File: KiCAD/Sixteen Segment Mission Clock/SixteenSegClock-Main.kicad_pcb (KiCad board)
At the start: 2 copper layers, 114.3 x 165.1 mm, 0 parts

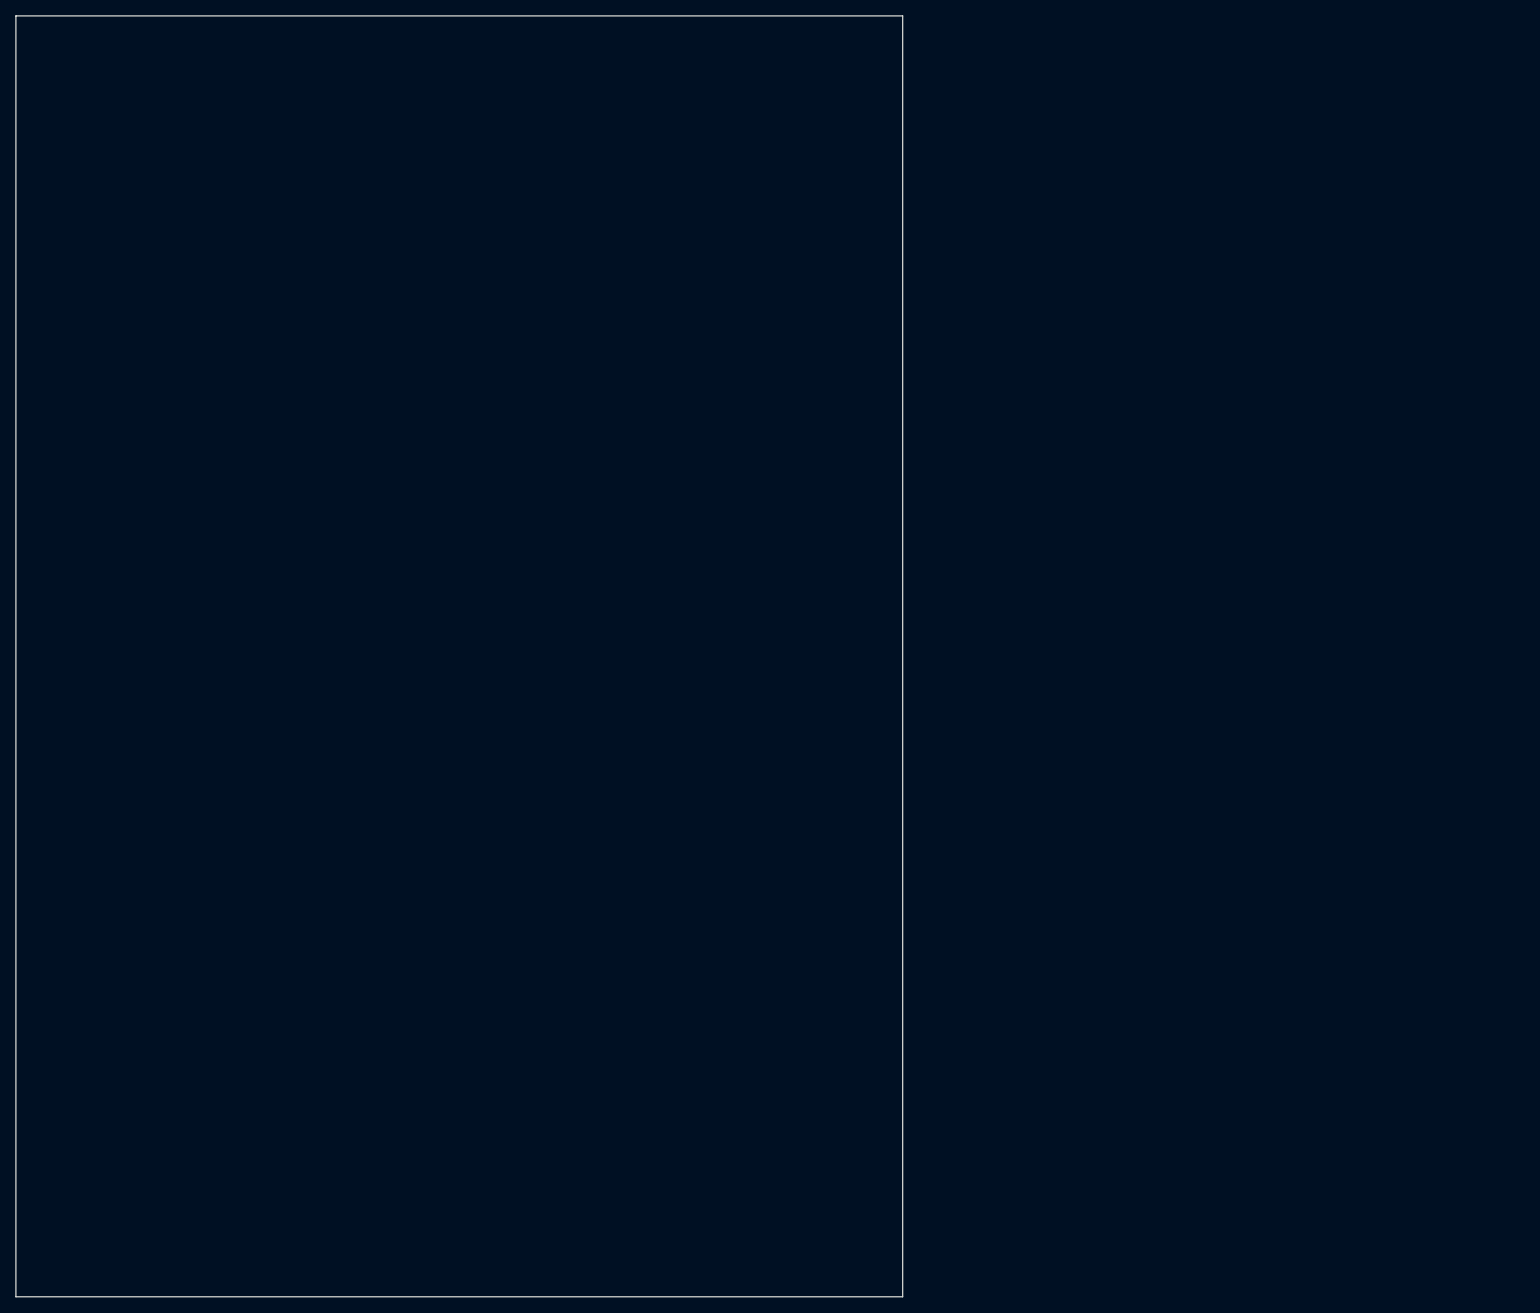
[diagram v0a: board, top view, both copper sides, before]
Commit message: Placed LEDs
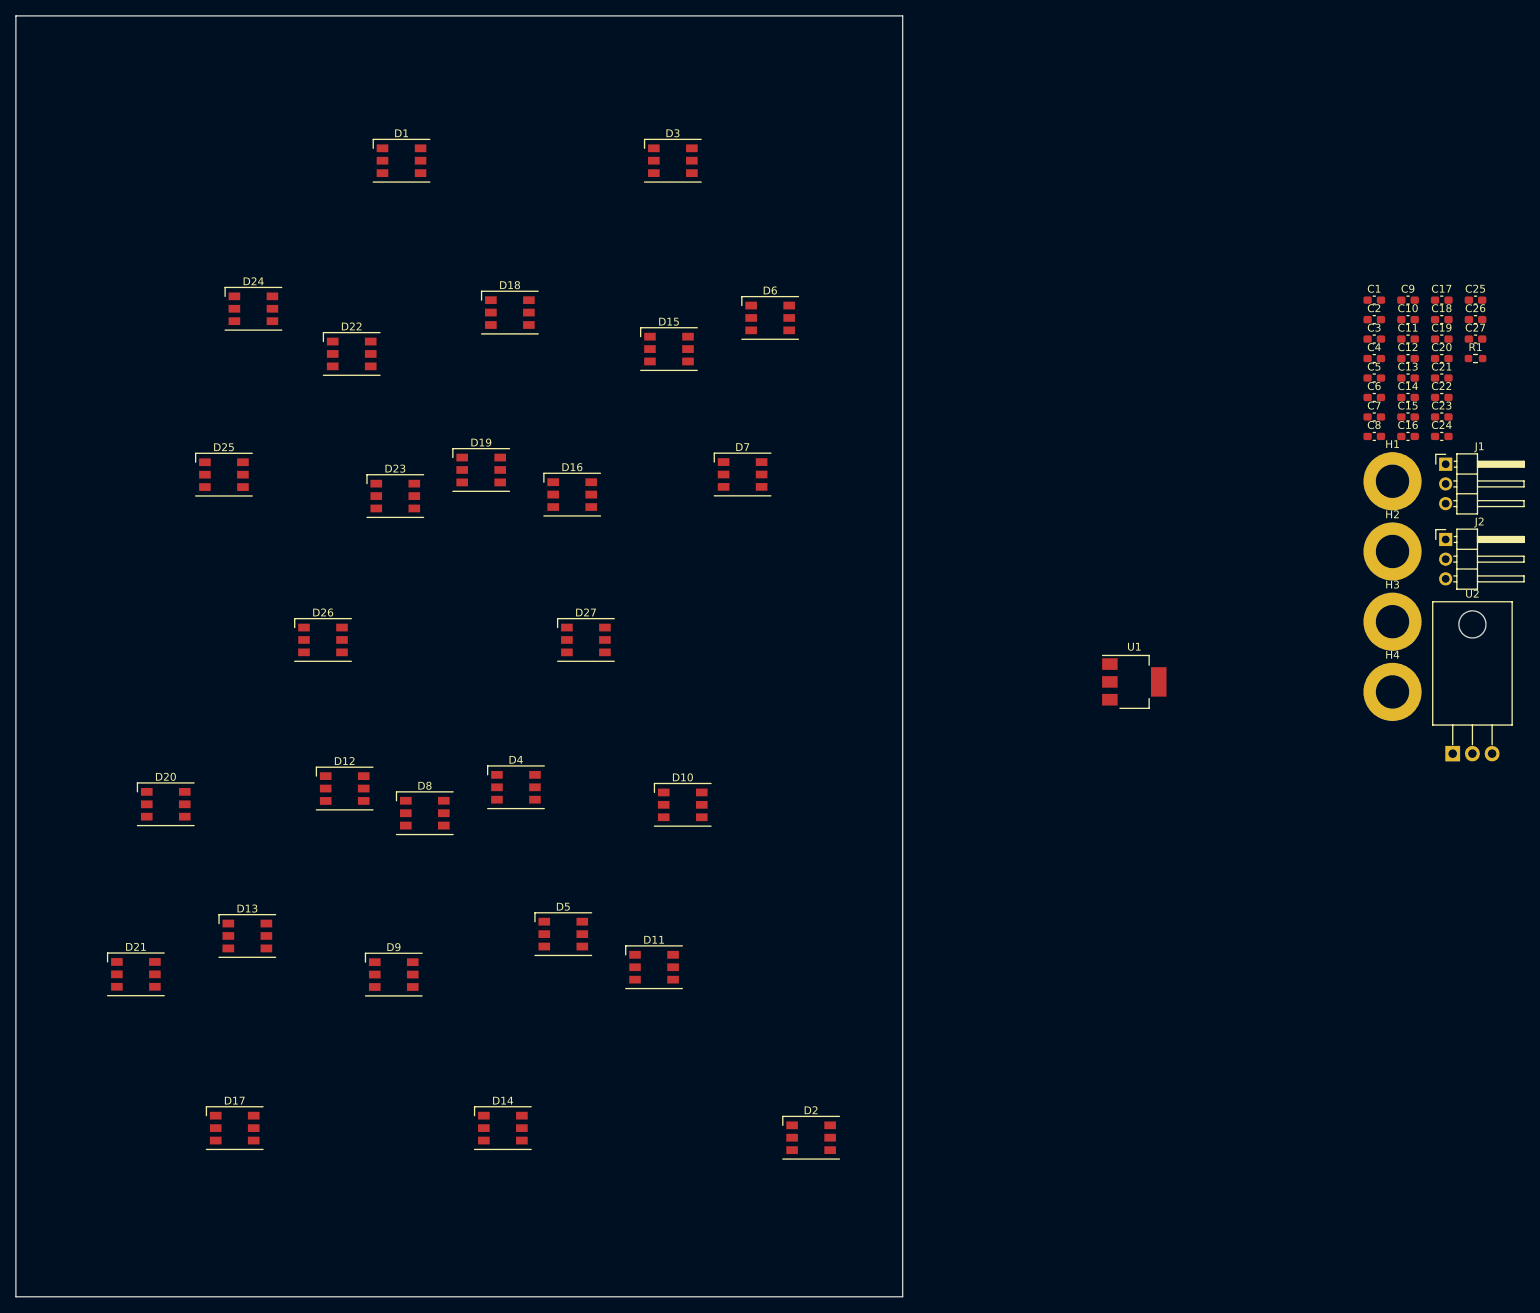
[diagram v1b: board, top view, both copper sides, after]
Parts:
- added C1: 1uF, Capacitor_SMD:C_0603_1608Metric_Pad1.08x0.95mm_HandSolder, F.Cu at (214.0, 65.0)
- added C10: 10uF, Capacitor_SMD:C_0603_1608Metric_Pad1.08x0.95mm_HandSolder, F.Cu at (218.4, 67.5)
- added C11: 10uF, Capacitor_SMD:C_0603_1608Metric_Pad1.08x0.95mm_HandSolder, F.Cu at (218.4, 70.1)
- added C12: 1uF, Capacitor_SMD:C_0603_1608Metric_Pad1.08x0.95mm_HandSolder, F.Cu at (218.4, 72.6)
- added C13: 1uF, Capacitor_SMD:C_0603_1608Metric_Pad1.08x0.95mm_HandSolder, F.Cu at (218.4, 75.1)
- added C14: 1uF, Capacitor_SMD:C_0603_1608Metric_Pad1.08x0.95mm_HandSolder, F.Cu at (218.4, 77.6)
- added C15: 1uF, Capacitor_SMD:C_0603_1608Metric_Pad1.08x0.95mm_HandSolder, F.Cu at (218.4, 80.1)
- added C16: 1uF, Capacitor_SMD:C_0603_1608Metric_Pad1.08x0.95mm_HandSolder, F.Cu at (218.4, 82.6)
- added C17: 1uF, Capacitor_SMD:C_0603_1608Metric_Pad1.08x0.95mm_HandSolder, F.Cu at (222.7, 65.0)
- added C18: 1uF, Capacitor_SMD:C_0603_1608Metric_Pad1.08x0.95mm_HandSolder, F.Cu at (222.7, 67.5)
- added C19: 1uF, Capacitor_SMD:C_0603_1608Metric_Pad1.08x0.95mm_HandSolder, F.Cu at (222.7, 70.1)
- added C2: 1uF, Capacitor_SMD:C_0603_1608Metric_Pad1.08x0.95mm_HandSolder, F.Cu at (214.0, 67.5)
- added C20: 1uF, Capacitor_SMD:C_0603_1608Metric_Pad1.08x0.95mm_HandSolder, F.Cu at (222.7, 72.6)
- added C21: 1uF, Capacitor_SMD:C_0603_1608Metric_Pad1.08x0.95mm_HandSolder, F.Cu at (222.7, 75.1)
- added C22: 1uF, Capacitor_SMD:C_0603_1608Metric_Pad1.08x0.95mm_HandSolder, F.Cu at (222.7, 77.6)
- added C23: 1uF, Capacitor_SMD:C_0603_1608Metric_Pad1.08x0.95mm_HandSolder, F.Cu at (222.7, 80.1)
- added C24: 1uF, Capacitor_SMD:C_0603_1608Metric_Pad1.08x0.95mm_HandSolder, F.Cu at (222.7, 82.6)
- added C25: 1uF, Capacitor_SMD:C_0603_1608Metric_Pad1.08x0.95mm_HandSolder, F.Cu at (227.1, 65.0)
- added C26: 1uF, Capacitor_SMD:C_0603_1608Metric_Pad1.08x0.95mm_HandSolder, F.Cu at (227.1, 67.5)
- added C27: 1uF, Capacitor_SMD:C_0603_1608Metric_Pad1.08x0.95mm_HandSolder, F.Cu at (227.1, 70.1)
- added C3: 1uF, Capacitor_SMD:C_0603_1608Metric_Pad1.08x0.95mm_HandSolder, F.Cu at (214.0, 70.1)
- added C4: 10uF, Capacitor_SMD:C_0603_1608Metric_Pad1.08x0.95mm_HandSolder, F.Cu at (214.0, 72.6)
- added C5: 1uF, Capacitor_SMD:C_0603_1608Metric_Pad1.08x0.95mm_HandSolder, F.Cu at (214.0, 75.1)
- added C6: 1uF, Capacitor_SMD:C_0603_1608Metric_Pad1.08x0.95mm_HandSolder, F.Cu at (214.0, 77.6)
- added C7: 10uF, Capacitor_SMD:C_0603_1608Metric_Pad1.08x0.95mm_HandSolder, F.Cu at (214.0, 80.1)
- added C8: 1uF, Capacitor_SMD:C_0603_1608Metric_Pad1.08x0.95mm_HandSolder, F.Cu at (214.0, 82.6)
- added C9: 1uF, Capacitor_SMD:C_0603_1608Metric_Pad1.08x0.95mm_HandSolder, F.Cu at (218.4, 65.0)
- added D1: WS2813B, LED_SMD:LED_WS2812_PLCC6_5.0x5.0mm_P1.6mm, F.Cu at (88.6, 47.1)
- added D10: WS2813B, LED_SMD:LED_WS2812_PLCC6_5.0x5.0mm_P1.6mm, F.Cu at (124.9, 130.1)
- added D11: WS2813B, LED_SMD:LED_WS2812_PLCC6_5.0x5.0mm_P1.6mm, F.Cu at (121.2, 151.0)
- added D12: WS2813B, LED_SMD:LED_WS2812_PLCC6_5.0x5.0mm_P1.6mm, F.Cu at (81.3, 128.0)
- added D13: WS2813B, LED_SMD:LED_WS2812_PLCC6_5.0x5.0mm_P1.6mm, F.Cu at (68.8, 147.0)
- added D14: WS2813B, LED_SMD:LED_WS2812_PLCC6_5.0x5.0mm_P1.6mm, F.Cu at (101.7, 171.8)
- added D15: WS2813B, LED_SMD:LED_WS2812_PLCC6_5.0x5.0mm_P1.6mm, F.Cu at (123.1, 71.3)
- added D16: WS2813B, LED_SMD:LED_WS2812_PLCC6_5.0x5.0mm_P1.6mm, F.Cu at (110.6, 90.1)
- added D17: WS2813B, LED_SMD:LED_WS2812_PLCC6_5.0x5.0mm_P1.6mm, F.Cu at (67.1, 171.8)
- added D18: WS2813B, LED_SMD:LED_WS2812_PLCC6_5.0x5.0mm_P1.6mm, F.Cu at (102.6, 66.6)
- added D19: WS2813B, LED_SMD:LED_WS2812_PLCC6_5.0x5.0mm_P1.6mm, F.Cu at (98.9, 86.9)
- added D2: WS2813B, LED_SMD:LED_WS2812_PLCC6_5.0x5.0mm_P1.6mm, F.Cu at (141.4, 173.0)
- added D20: WS2813B, LED_SMD:LED_WS2812_PLCC6_5.0x5.0mm_P1.6mm, F.Cu at (58.2, 130.0)
- added D21: WS2813B, LED_SMD:LED_WS2812_PLCC6_5.0x5.0mm_P1.6mm, F.Cu at (54.4, 151.9)
- added D22: WS2813B, LED_SMD:LED_WS2812_PLCC6_5.0x5.0mm_P1.6mm, F.Cu at (82.2, 72.0)
- added D23: WS2813B, LED_SMD:LED_WS2812_PLCC6_5.0x5.0mm_P1.6mm, F.Cu at (87.8, 90.3)
- added D24: WS2813B, LED_SMD:LED_WS2812_PLCC6_5.0x5.0mm_P1.6mm, F.Cu at (69.5, 66.2)
- added D25: WS2813B, LED_SMD:LED_WS2812_PLCC6_5.0x5.0mm_P1.6mm, F.Cu at (65.7, 87.5)
- added D26: WS2813B, LED_SMD:LED_WS2812_PLCC6_5.0x5.0mm_P1.6mm, F.Cu at (78.5, 108.8)
- added D27: WS2813B, LED_SMD:LED_WS2812_PLCC6_5.0x5.0mm_P1.6mm, F.Cu at (112.4, 108.8)
- added D3: WS2813B, LED_SMD:LED_WS2812_PLCC6_5.0x5.0mm_P1.6mm, F.Cu at (123.6, 47.1)
- added D4: WS2813B, LED_SMD:LED_WS2812_PLCC6_5.0x5.0mm_P1.6mm, F.Cu at (103.4, 127.8)
- added D5: WS2813B, LED_SMD:LED_WS2812_PLCC6_5.0x5.0mm_P1.6mm, F.Cu at (109.5, 146.8)
- added D6: WS2813B, LED_SMD:LED_WS2812_PLCC6_5.0x5.0mm_P1.6mm, F.Cu at (136.1, 67.3)
- added D7: WS2813B, LED_SMD:LED_WS2812_PLCC6_5.0x5.0mm_P1.6mm, F.Cu at (132.6, 87.5)
- added D8: WS2813B, LED_SMD:LED_WS2812_PLCC6_5.0x5.0mm_P1.6mm, F.Cu at (91.6, 131.2)
- added D9: WS2813B, LED_SMD:LED_WS2812_PLCC6_5.0x5.0mm_P1.6mm, F.Cu at (87.6, 152.0)
- added H1: M4, MountingHole:MountingHole_4.3mm_M4_DIN965_Pad, F.Cu at (216.4, 88.4)
- added H2: M4, MountingHole:MountingHole_4.3mm_M4_DIN965_Pad, F.Cu at (216.4, 97.4)
- added H3: M4, MountingHole:MountingHole_4.3mm_M4_DIN965_Pad, F.Cu at (216.4, 106.5)
- added H4: M4, MountingHole:MountingHole_4.3mm_M4_DIN965_Pad, F.Cu at (216.4, 115.5)
- added J1: Input, Connector_PinHeader_2.54mm:PinHeader_1x03_P2.54mm_Horizontal, F.Cu at (223.2, 86.2)
- added J2: Output, Connector_PinHeader_2.54mm:PinHeader_1x03_P2.54mm_Horizontal, F.Cu at (223.2, 95.9)
- added R1: 220Ω, Resistor_SMD:R_0603_1608Metric_Pad0.98x0.95mm_HandSolder, F.Cu at (227.1, 72.6)
- added U1: AZ1117-5.0, Package_TO_SOT_SMD:SOT-223-3_TabPin2, F.Cu at (183.1, 114.2)
- added U2: L78S05CV, Package_TO_SOT_THT:TO-220-3_Horizontal_TabDown, F.Cu at (224.1, 123.5)

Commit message: Initial routings
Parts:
- removed C20, C21, C22, C23, C24, C25, C26, C27: 1uF, Capacitor_SMD:C_0603_1608Metric_Pad1.08x0.95mm_HandSolder
- removed the U1 at (183.1, 114.2)
- C1, C2: value 1uF -> 10uF; moved to B.Cu
- C10, C11, C4, C7: value 10uF -> 1uF; moved to B.Cu
- C12, C13, C14, C15, C16, C17, C18, C19, C3, C5, C6, C8, C9, J1, J2, R1: moved to B.Cu
- U1: renamed from U2; moved to B.Cu
- moved H2 188.8 mm to (48.9, 184.4)
- moved H4 183.9 mm to (50.6, 35.8)
- moved C9 178.6 mm to (56.5, 140.5), turned to 180 degrees
- moved U1 175.2 mm to (53.1, 85.5), turned to 180 degrees
- moved R1 172.7 mm to (58.2, 108.8)
- moved J1 170.6 mm to (53.9, 106.3), turned to 180 degrees
- moved C2 169.9 mm to (45.7, 90.9), turned to 180 degrees
- moved C8 164.9 mm to (75.3, 171.8), turned to 180 degrees
- moved C1 161.9 mm to (54.1, 90.4), turned to 180 degrees
- moved C17 154.5 mm to (89.1, 142.5), turned to 180 degrees
- moved C16 154.0 mm to (74.9, 138.4), turned to 180 degrees
- moved C7 151.0 mm to (94.2, 172.0), turned to 180 degrees
- moved C10 150.3 mm to (68.4, 77.8), turned to 180 degrees
- moved C11 138.2 mm to (85.8, 109.0), turned to 180 degrees
- moved C18 136.7 mm to (105.9, 138.5), turned to 180 degrees
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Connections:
- C1 pad 1: /V5_0 -> /VIN_12V
- C10 pad 1: /VIN_12V -> /V5_0
- C4 pad 1: /VIN_12V -> /V5_0
- D1 pad 5: Net-(D1-GND) -> /GND
- D10 pad 5: Net-(D1-GND) -> /GND
- D11 pad 5: Net-(D1-GND) -> /GND
- D12 pad 5: Net-(D1-GND) -> /GND
- D13 pad 5: Net-(D1-GND) -> /GND
- D14 pad 5: Net-(D1-GND) -> /GND
- D15 pad 5: Net-(D1-GND) -> /GND
- D16 pad 5: Net-(D1-GND) -> /GND
- D17 pad 5: Net-(D1-GND) -> /GND
- D18 pad 5: Net-(D1-GND) -> /GND
- D19 pad 5: Net-(D1-GND) -> /GND
- D2 pad 5: Net-(D1-GND) -> /GND
- D20 pad 5: Net-(D1-GND) -> /GND
- D21 pad 5: Net-(D1-GND) -> /GND
- D22 pad 5: Net-(D1-GND) -> /GND
- D23 pad 5: Net-(D1-GND) -> /GND
- D24 pad 5: Net-(D1-GND) -> /GND
- D25 pad 5: Net-(D1-GND) -> /GND
- D26 pad 5: Net-(D1-GND) -> /GND
- D27 pad 5: Net-(D1-GND) -> /GND
- D3 pad 5: Net-(D1-GND) -> /GND
- D4 pad 5: Net-(D1-GND) -> /GND
- D5 pad 5: Net-(D1-GND) -> /GND
- D6 pad 5: Net-(D1-GND) -> /GND
- D7 pad 5: Net-(D1-GND) -> /GND
- D8 pad 5: Net-(D1-GND) -> /GND
- D9 pad 5: Net-(D1-GND) -> /GND
- H1 pad 1: Net-(D1-GND) -> /GND
- H2 pad 1: Net-(D1-GND) -> /GND
- H3 pad 1: Net-(D1-GND) -> /GND
- H4 pad 1: Net-(D1-GND) -> /GND
- J1 pad 3: Net-(D1-GND) -> /GND
- J2 pad 1: Net-(D1-GND) -> /GND
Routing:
- net /E-F: track 0.00 -> 116.1 mm
- net /B-C: track 0.00 -> 105.1 mm
- net /K-L: track 0.00 -> 100.8 mm
- net /H-I: track 0.00 -> 96.3 mm
- net /I-J: track 0.00 -> 86.8 mm
- net /VIN_12V: track 0.00 -> 84.9 mm
- net /L-M: track 0.00 -> 83.2 mm
- net /J-K: track 0.00 -> 67.4 mm
- net /C-D2: track 0.00 -> 60.8 mm
- net /G2-H: track 0.00 -> 60.4 mm
- net /D1-E: track 0.00 -> 58.8 mm
- net /A2-B: track 0.00 -> 52.5 mm
- net /D2-D1: track 0.00 -> 46.2 mm
- net /A1-A2: track 0.00 -> 45.5 mm
- net /G1-G2: track 0.00 -> 45.4 mm
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- added copper zone on B.Cu, net /GND
- added copper zone on F.Cu, net /GND

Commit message: Routed all components
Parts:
- moved C2 30.5 mm to (53.0, 61.3), turned to 90 degrees
- moved C1 29.7 mm to (48.0, 61.3), turned to 90 degrees
- moved U1 19.2 mm to (47.9, 67.0), turned to 0 degrees
- moved C19 5.46 mm to (139.5, 170.2), turned to -110 degrees
- moved C8 3.16 mm to (72.2, 172.4), turned to -90 degrees
- moved C18 3.01 mm to (108.2, 136.7), turned to 20 degrees
- moved C10 2.92 mm to (65.8, 76.5), turned to -10 degrees
- moved C17 2.43 mm to (91.4, 141.9), turned to -10 degrees
- moved C7 2.41 mm to (96.6, 172.4), turned to 90 degrees
- moved C14 2.33 mm to (102.7, 77.2), turned to -10 degrees
- moved C16 2.30 mm to (73.6, 136.5), turned to -35 degrees
- moved C6 2.29 mm to (124.9, 140.9), turned to -10 degrees
- moved C11 2.19 mm to (83.6, 109.3), turned to 90 degrees
- moved C12 2.03 mm to (107.2, 109.1), turned to -90 degrees
- moved C9 2.02 mm to (54.5, 140.7), turned to -10 degrees
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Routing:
- net /V5_0: track 0.00 -> 681.8 mm, vias 0 -> 27
- net /GND: track 0.00 -> 321.2 mm, vias 0 -> 34
- net /VIN_12V: track 84.9 -> 4.81 mm
- net /DATA_IN: track 0.00 -> 77.0 mm, vias 0 -> 1
- net /DATA_OUT: track 0.00 -> 70.1 mm
- net /M-DP: track 31.4 -> 87.6 mm, vias 0 -> 2
- net /J-K: track 67.4 -> 114.8 mm, vias 0 -> 2
- net /F-G1: track 36.4 -> 72.1 mm, vias 0 -> 2
- net /H-I: track 96.3 -> 114.1 mm
- net /A2-B: track 52.5 -> 67.1 mm
- net /K-L: track 100.8 -> 111.2 mm
- net /E-F: track 116.1 -> 124.3 mm
- net /G1-G2: track 45.4 -> 50.8 mm
- net /D2-D1: track 46.2 -> 51.3 mm
- net /L-M: track 83.2 -> 88.1 mm
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- added copper zone on B.Cu, net /VIN_12V
